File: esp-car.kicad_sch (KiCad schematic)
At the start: 32 parts, among them J1 Conn_01x07_Socket, J2 Conn_01x07_Socket, U1 ESP32-DEVKIT-V1, U3 L293D

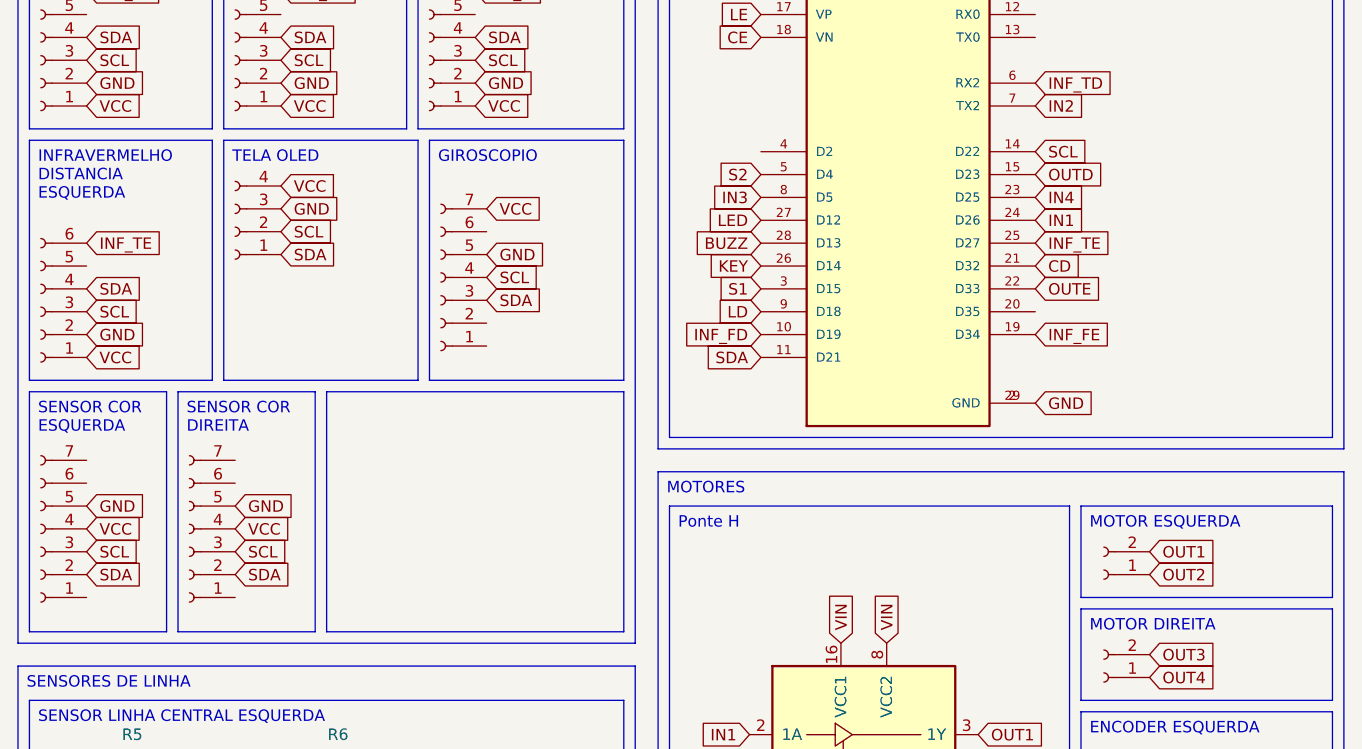
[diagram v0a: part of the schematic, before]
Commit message: esp-car 3.2
trilhas de cimas feitas, precisa arrumar resistores
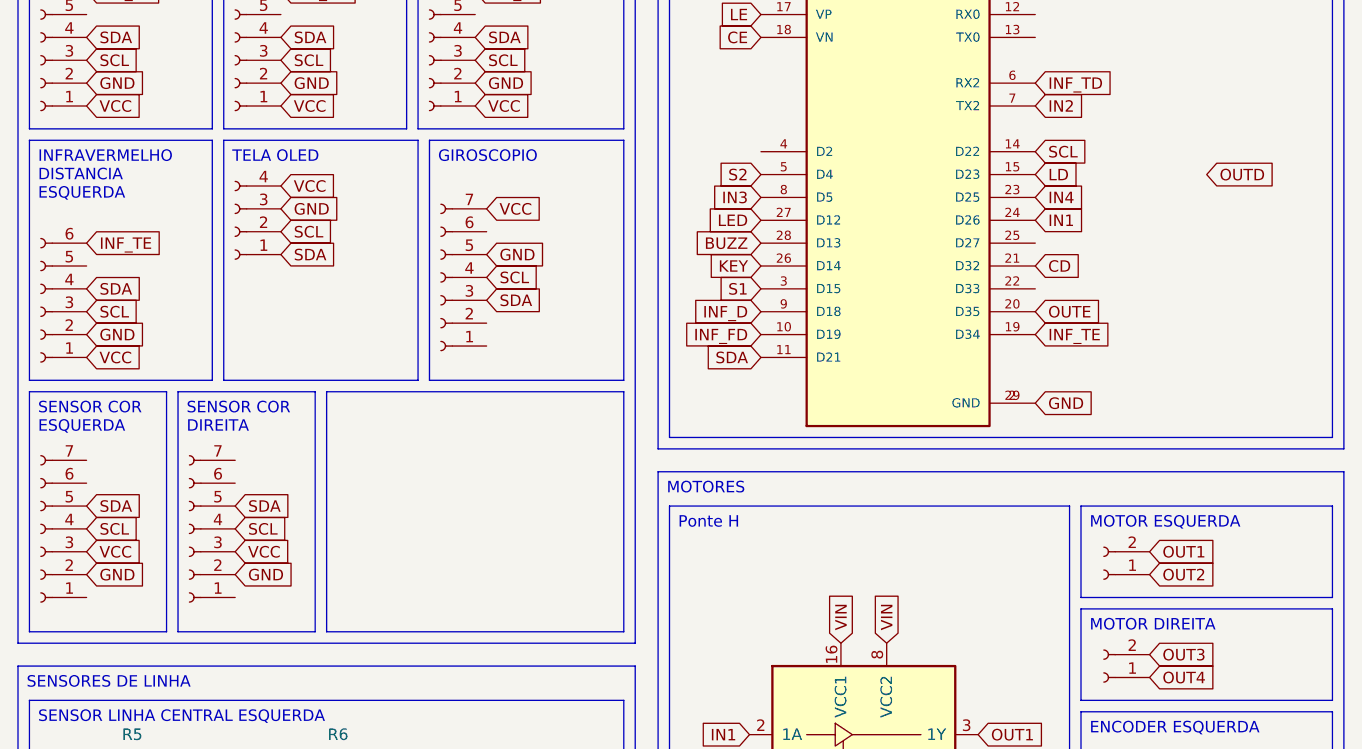
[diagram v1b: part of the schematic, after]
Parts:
- R6: footprint Resistor_THT:R_Axial_DIN0204_L3.6mm_D1.6mm_P2.54mm_Vertical -> Resistor_THT:R_Axial_DIN0204_L3.6mm_D1.6mm_P5.08mm_Horizontal
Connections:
- net 3.3V: now also J1.3 (Pin_3), J2.3 (Pin_3); no longer J1.4 (Pin_4), J2.4 (Pin_4)
- net GND: now also J1.2 (Pin_2), J2.2 (Pin_2); no longer J1.5 (Pin_5), J2.5 (Pin_5)
- net INF_D: now also U1.9 (D18)
- net INF_FE: no longer U1.19 (D34)
- net INF_TE: now also U1.19 (D34); no longer U1.25 (D27)
- net LD: now also U1.15 (D23); no longer U1.9 (D18)
- net OUTD: no longer U1.15 (D23)
- net OUTE: now also U1.20 (D35); no longer U1.22 (D33)
- net SCL: now also J1.4 (Pin_4), J2.4 (Pin_4); no longer J1.3 (Pin_3), J2.3 (Pin_3)
- net SDA: now also J1.5 (Pin_5), J2.5 (Pin_5); no longer J1.2 (Pin_2), J2.2 (Pin_2)
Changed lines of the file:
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@@
 	(global_label "GND"
 		(shape input)
-		(at 21.59 86.36 0)
+		(at 21.59 93.98 0)
 		(fields_autoplaced yes)
 		(effects
@@
 		)
 		(property "Intersheetrefs" "${INTERSHEET_REFS}"
-			(at 28.4457 86.36 0)
+			(at 28.4457 93.98 0)
 			(effects
 				(font
@@
 	(global_label "VCC"
 		(shape input)
-		(at 38.1 88.9 0)
+		(at 38.1 91.44 0)
 		(fields_autoplaced yes)
 		(effects
@@
 		)
 		(property "Intersheetrefs" "${INTERSHEET_REFS}"
-			(at 44.7138 88.9 0)
+			(at 44.7138 91.44 0)
 			(effects
 				(font
@@
 	(global_label "GND"
 		(shape input)
-		(at 38.1 86.36 0)
+		(at 38.1 93.98 0)
 		(fields_autoplaced yes)
 		(effects
@@
 		)
 		(property "Intersheetrefs" "${INTERSHEET_REFS}"
-			(at 44.9557 86.36 0)
+			(at 44.9557 93.98 0)
 			(effects
 				(font
@@
 	(global_label "LD"
 		(shape input)
-		(at 96.52 64.77 180)
+		(at 127 49.53 0)
 		(fields_autoplaced yes)
 		(effects
@@
 				(size 1.27 1.27)
 			)
-			(justify right)
+			(justify left)
 		)
 		(property "Intersheetrefs" "${INTERSHEET_REFS}"
-			(at 91.2367 64.77 0)
+			(at 132.2833 49.53 0)
 			(effects
 				(font
 					(size 1.27 1.27)
 				)
-				(justify right)
+				(justify left)
 				(hide yes)
 			)
@@
 		)
 	)
+	(global_label "INF_D"
+		(shape input)
+		(at 96.52 64.77 180)
+		(fields_autoplaced yes)
+		(effects
+			(font
+				(size 1.27 1.27)
+			)
+			(justify right)
+		)
+		(property "Intersheetrefs" "${INTERSHEET_REFS}"
+			(at 88.2733 64.77 0)
+			(effects
+				(font
+					(size 1.27 1.27)
+				)
+				(justify right)
+				(hide yes)
+			)
+		)
+	)
 	(global_label "INF_FD"
 		(shape input)
@@
 	(global_label "SDA"
 		(shape input)
-		(at 21.59 93.98 0)
+		(at 21.59 86.36 0)
 		(fields_autoplaced yes)
 		(effects
@@
 		)
 		(property "Intersheetrefs" "${INTERSHEET_REFS}"
-			(at 28.1433 93.98 0)
+			(at 28.1433 86.36 0)
 			(effects
 				(font
@@
 	(global_label "SCL"
 		(shape input)
-		(at 38.1 91.44 0)
+		(at 38.1 88.9 0)
 		(fields_autoplaced yes)
 		(effects
@@
 		)
 		(property "Intersheetrefs" "${INTERSHEET_REFS}"
-			(at 44.5928 91.44 0)
+			(at 44.5928 88.9 0)
 			(effects
 				(font
@@
 	(global_label "SDA"
 		(shape input)
-		(at 38.1 93.98 0)
+		(at 38.1 86.36 0)
 		(fields_autoplaced yes)
 		(effects
@@
 		)
 		(property "Intersheetrefs" "${INTERSHEET_REFS}"
-			(at 44.6533 93.98 0)
+			(at 44.6533 86.36 0)
 			(effects
 				(font
@@
 	(global_label "VCC"
 		(shape input)
-		(at 21.59 88.9 0)
+		(at 21.59 91.44 0)
 		(fields_autoplaced yes)
 		(effects
@@
 		)
 		(property "Intersheetrefs" "${INTERSHEET_REFS}"
-			(at 28.2038 88.9 0)
+			(at 28.2038 91.44 0)
 			(effects
 				(font
@@
 	(global_label "SCL"
 		(shape input)
-		(at 21.59 91.44 0)
+		(at 21.59 88.9 0)
 		(fields_autoplaced yes)
 		(effects
@@
 		)
 		(property "Intersheetrefs" "${INTERSHEET_REFS}"
-			(at 28.0828 91.44 0)
+			(at 28.0828 88.9 0)
 			(effects
 				(font
@@
 	(global_label "INF_TE"
 		(shape input)
-		(at 127 57.15 0)
+		(at 127 67.31 0)
 		(fields_autoplaced yes)
 		(effects
@@
 		)
 		(property "Intersheetrefs" "${INTERSHEET_REFS}"
-			(at 136.0933 57.15 0)
+			(at 136.0933 67.31 0)
 			(effects
 				(font
@@
 	(global_label "OUTE"
 		(shape input)
-		(at 127 62.23 0)
+		(at 127 64.77 0)
 		(fields_autoplaced yes)
 		(effects
@@
 		)
 		(property "Intersheetrefs" "${INTERSHEET_REFS}"
-			(at 134.7628 62.23 0)
+			(at 134.7628 64.77 0)
 			(effects
 				(font
@@
 		)
 	)
-	(global_label "INF_FE"
-		(shape input)
-		(at 127 67.31 0)
-		(fields_autoplaced yes)
-		(effects
-			(font
-				(size 1.27 1.27)
-			)
-			(justify left)
-		)
-		(property "Intersheetrefs" "${INTERSHEET_REFS}"
-			(at 136.2143 67.31 0)
-			(effects
-				(font
-					(size 1.27 1.27)
-				)
-				(justify left)
-				(hide yes)
-			)
-		)
-	)
 	(global_label "GND"
 		(shape input)
@@
 	(global_label "OUTD"
 		(shape input)
-		(at 127 49.53 0)
+		(at 146.05 49.53 0)
 		(fields_autoplaced yes)
 		(effects
@@
 		)
 		(property "Intersheetrefs" "${INTERSHEET_REFS}"
-			(at 134.8838 49.53 0)
+			(at 153.9338 49.53 0)
 			(effects
 				(font
@@
 			)
 		)
-		(property "Footprint" "Resistor_THT:R_Axial_DIN0204_L3.6mm_D1.6mm_P2.54mm_Vertical"
+		(property "Footprint" "Resistor_THT:R_Axial_DIN0204_L3.6mm_D1.6mm_P5.08mm_Horizontal"
 			(at 49.53 119.888 90)
 			(effects

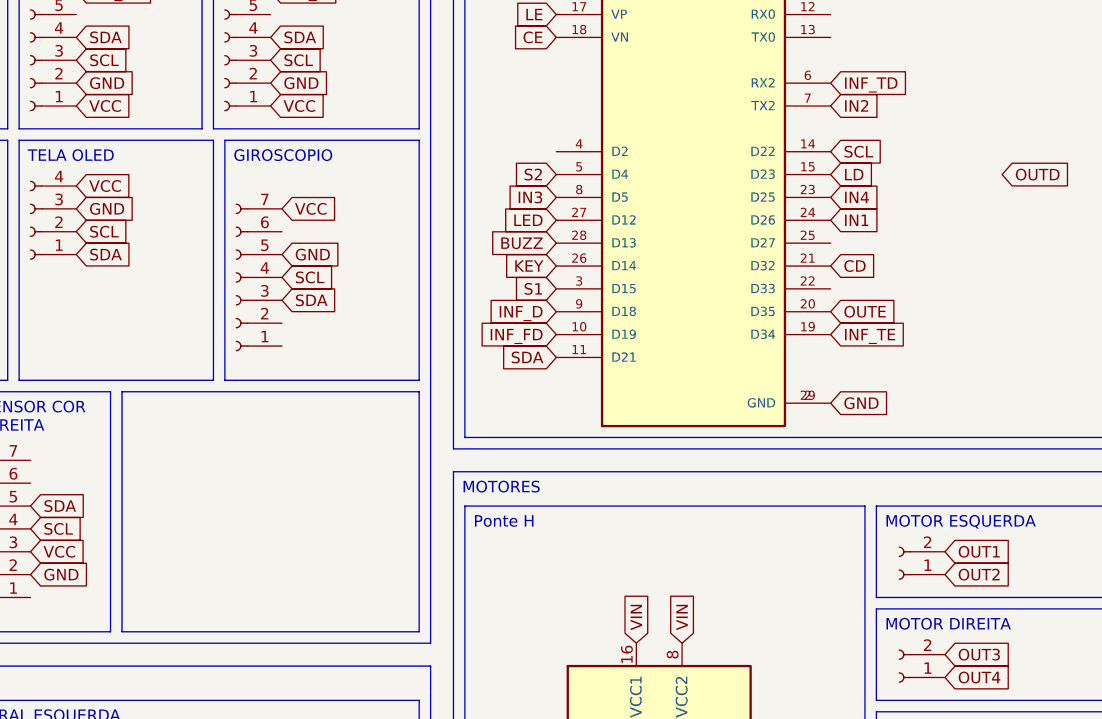
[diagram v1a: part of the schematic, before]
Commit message: esp-car 3.3
furação mais metade da parte de baixo completa
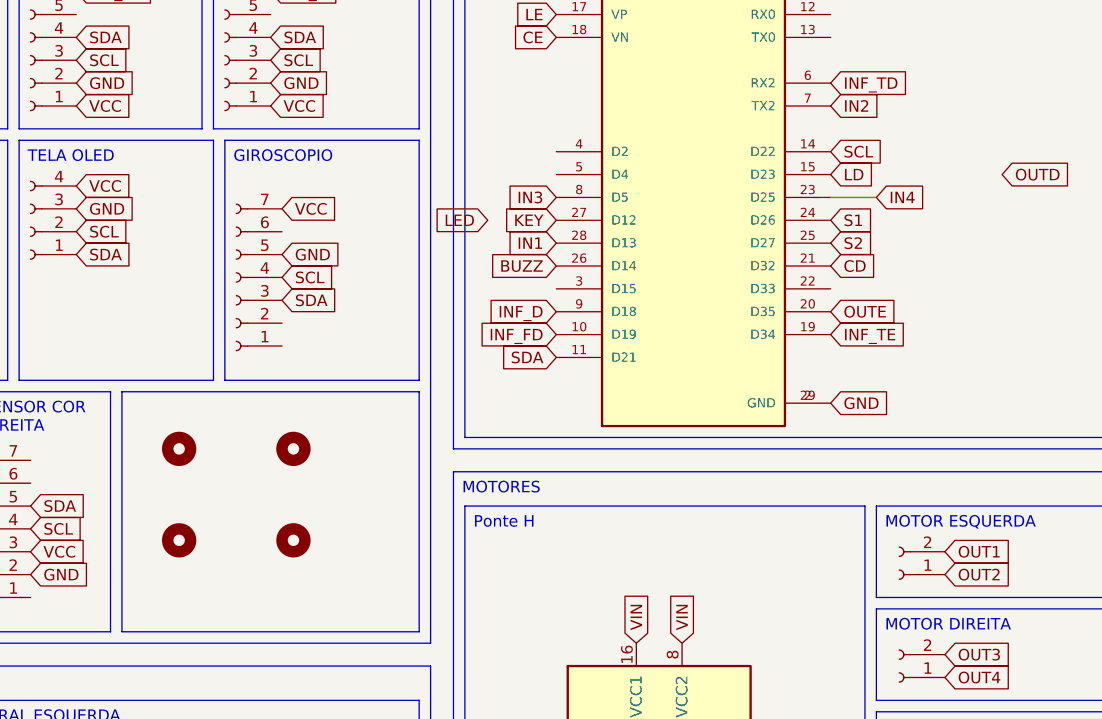
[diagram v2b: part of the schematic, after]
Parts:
- added H1, H2, H3, H4: MountingHole, MountingHole:MountingHole_3.2mm_M3, symbol Mechanical:MountingHole
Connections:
- net BUZZ: now also U1.26 (D14); no longer U1.28 (D13)
- net IN1: now also U1.28 (D13); no longer U1.24 (D26)
- net KEY: now also U1.27 (D12); no longer U1.26 (D14)
- net LED: no longer U1.27 (D12)
- net S1: now also U1.24 (D26); no longer U1.3 (D15)
- net S2: now also U1.25 (D27); no longer U1.5 (D4)
